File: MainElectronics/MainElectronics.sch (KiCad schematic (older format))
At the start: 15 parts

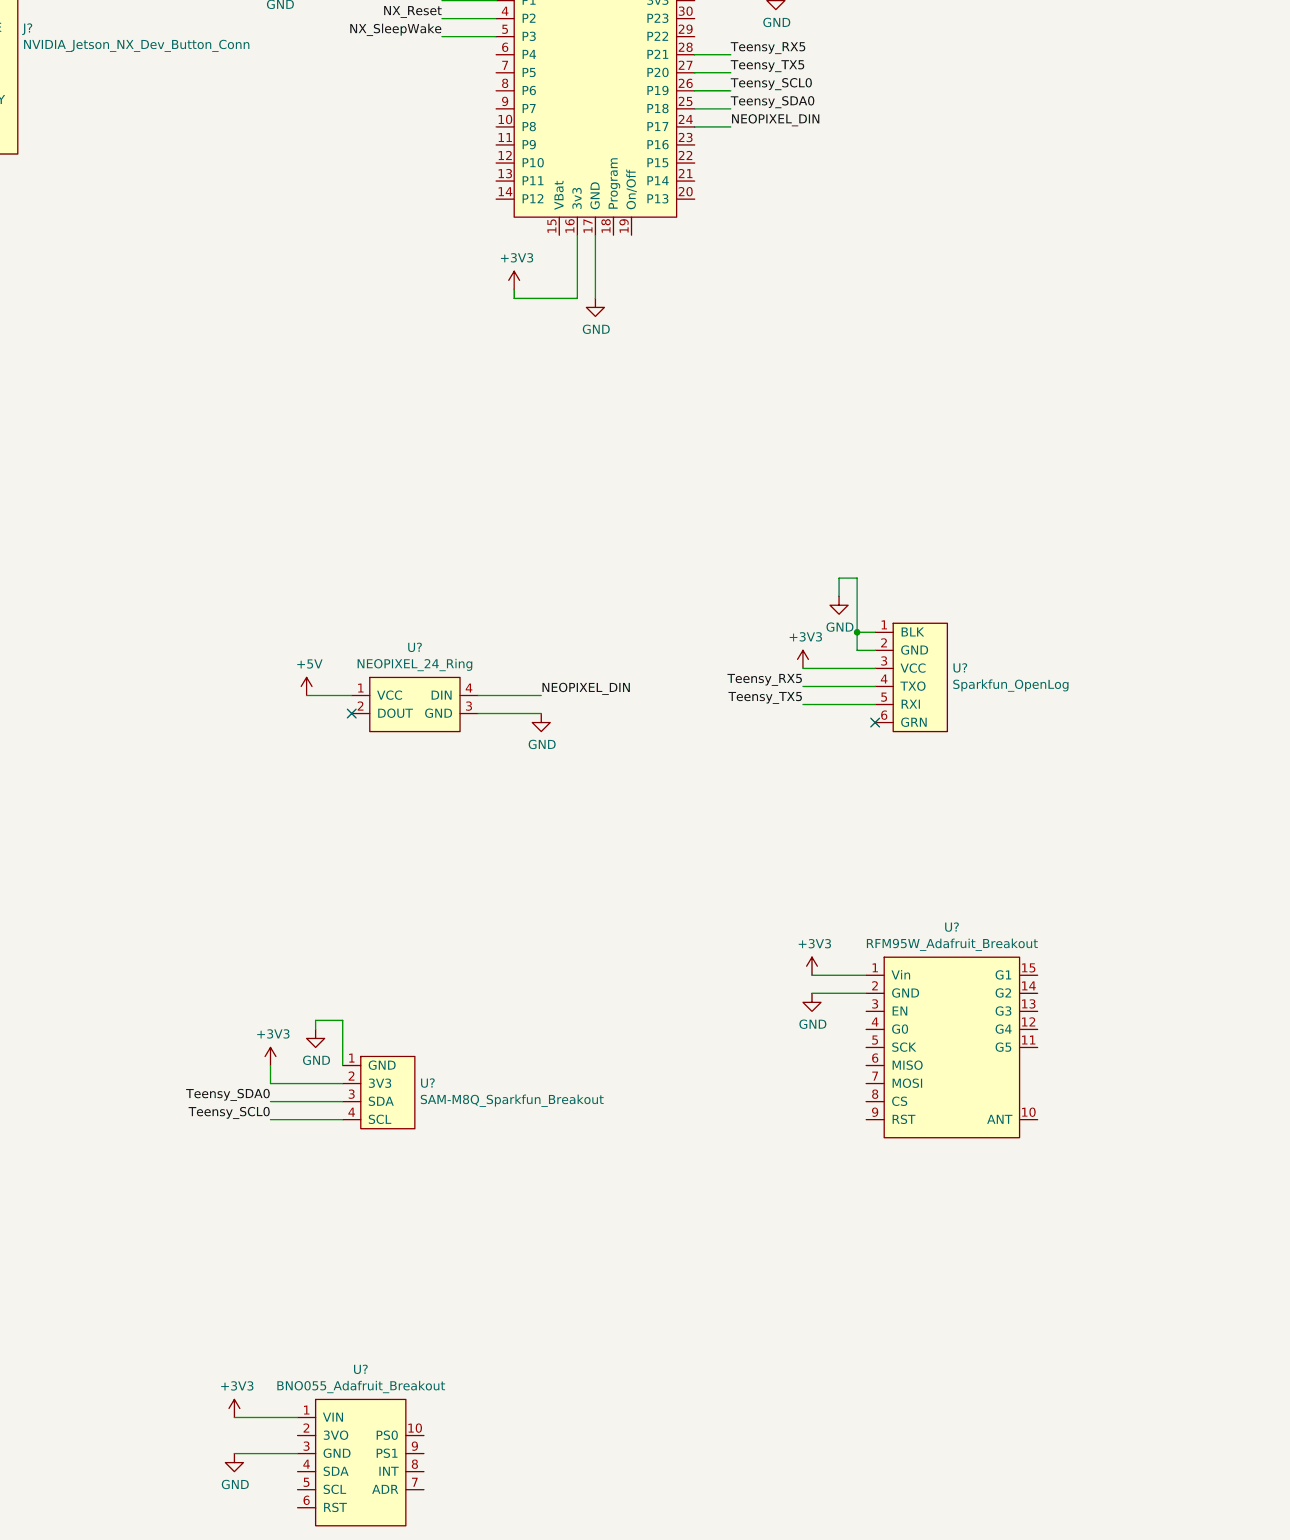
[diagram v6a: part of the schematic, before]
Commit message: Finished BNO055 and RFM95W
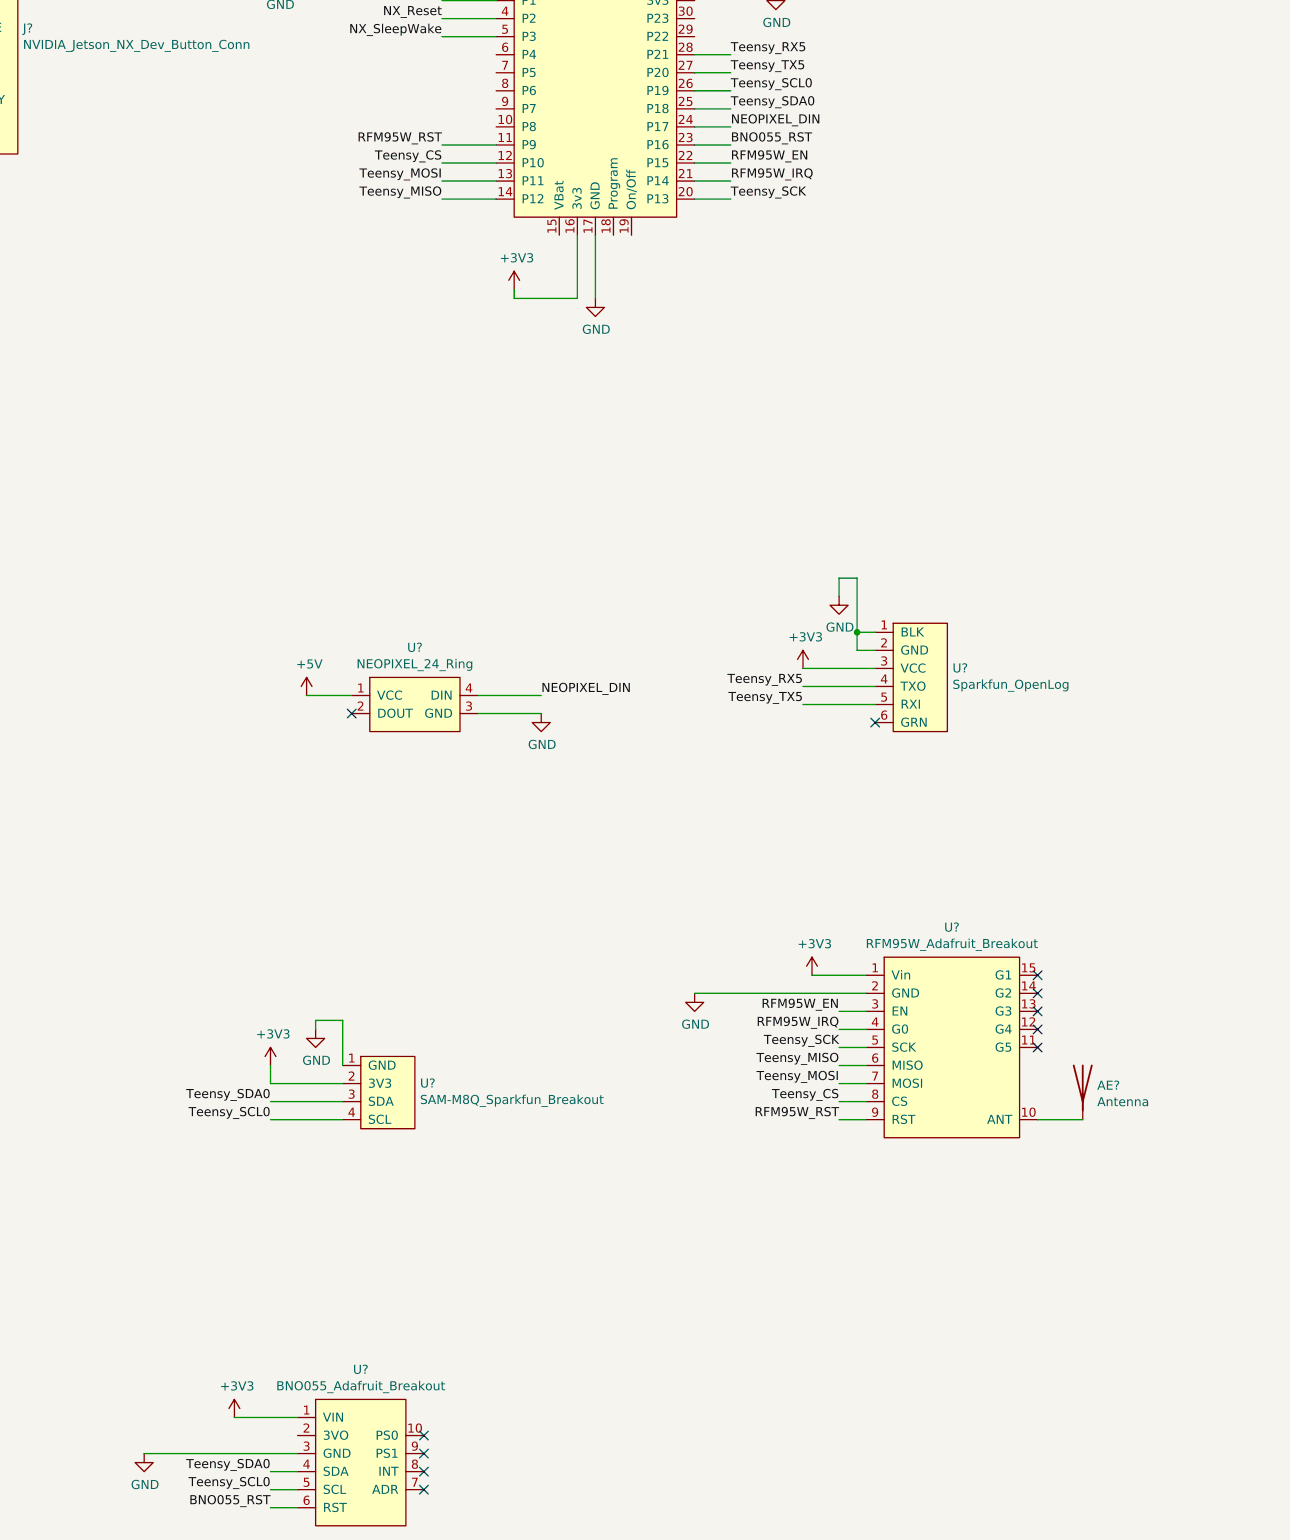
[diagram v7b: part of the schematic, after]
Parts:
- added AE?: Antenna, symbol Device:Antenna
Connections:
- net Teensy_SCL0: now also U?.5 (SCL)
- net Teensy_SDA0: now also U?.4 (SDA)
- net at U?.10 (ANT): now also AE?.1 (A)
- net RFM95W_EN: now reaches U?.3 (EN)
- net RFM95W_EN: now also U?.22 (P15)
- net RFM95W_IRQ: now reaches U?.4 (G0)
- net RFM95W_IRQ: now also U?.21 (P14)
- net Teensy_SCK: now reaches U?.5 (SCK)
- net Teensy_SCK: now also U?.20 (P13)
- net Teensy_MISO: now reaches U?.6 (MISO)
- net Teensy_MISO: now also U?.14 (P12)
- net Teensy_MOSI: now reaches U?.7 (MOSI)
- net Teensy_MOSI: now also U?.13 (P11)
- net Teensy_CS: now reaches U?.8 (CS)
- net Teensy_CS: now also U?.12 (P10)
- net RFM95W_RST: now reaches U?.9 (RST)
- net RFM95W_RST: now also U?.11 (P9)
- net BNO055_RST: now reaches U?.6 (RST)
- net BNO055_RST: now also U?.23 (P16)
- no-connect marks 4 -> 13
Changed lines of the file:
@@
 L power:GND #PWR?
 U 1 1 5EE0F934
-P 11500 7800
-F 0 "#PWR?" H 11500 7550 50  0001 C CNN
-F 1 "GND" H 11505 7627 50  0000 C CNN
-F 2 "" H 11500 7800 50  0001 C CNN
-F 3 "" H 11500 7800 50  0001 C CNN
-	1    11500 7800
-	1    0    0    -1
-$EndComp
-Wire Wire Line
-	11500 7800 11800 7800
+P 10850 7800
+F 0 "#PWR?" H 10850 7550 50  0001 C CNN
+F 1 "GND" H 10855 7627 50  0000 C CNN
+F 2 "" H 10850 7800 50  0001 C CNN
+F 3 "" H 10850 7800 50  0001 C CNN
+	1    10850 7800
+	1    0    0    -1
+$EndComp
+Wire Wire Line
+	10850 7800 11800 7800
 $Comp
 L power:+3V3 #PWR?
@@
 L power:GND #PWR?
 U 1 1 5EE15824
-P 8300 10350
-F 0 "#PWR?" H 8300 10100 50  0001 C CNN
-F 1 "GND" H 8305 10177 50  0000 C CNN
-F 2 "" H 8300 10350 50  0001 C CNN
-F 3 "" H 8300 10350 50  0001 C CNN
-	1    8300 10350
-	1    0    0    -1
-$EndComp
-Wire Wire Line
-	8650 10350 8300 10350
+P 7800 10350
+F 0 "#PWR?" H 7800 10100 50  0001 C CNN
+F 1 "GND" H 7805 10177 50  0000 C CNN
+F 2 "" H 7800 10350 50  0001 C CNN
+F 3 "" H 7800 10350 50  0001 C CNN
+	1    7800 10350
+	1    0    0    -1
+$EndComp
+Wire Wire Line
+	8650 10350 7800 10350
 Wire Wire Line
 	11850 6100 11450 6100
@@
 Text Label 8500 8400 2    50   ~ 0
 Teensy_SDA0
+Text Label 8500 10550 2    50   ~ 0
+Teensy_SCL0
+Wire Wire Line
+	8500 10550 8650 10550
+Text Label 8500 10450 2    50   ~ 0
+Teensy_SDA0
+Wire Wire Line
+	8500 10450 8650 10450
+Text Label 8500 10650 2    50   ~ 0
+BNO055_RST
+Wire Wire Line
+	8500 10650 8650 10650
+Text Label 11050 3100 0    50   ~ 0
+BNO055_RST
+Wire Wire Line
+	11050 3100 10850 3100
+Text Label 9450 3200 2    50   ~ 0
+Teensy_CS
+Text Label 9450 3300 2    50   ~ 0
+Teensy_MOSI
+Text Label 9450 3400 2    50   ~ 0
+Teensy_MISO
+Text Label 11050 3400 0    50   ~ 0
+Teensy_SCK
+Wire Wire Line
+	11050 3400 10850 3400
+Wire Wire Line
+	9750 3400 9450 3400
+Wire Wire Line
+	9450 3300 9750 3300
+Wire Wire Line
+	9750 3200 9450 3200
+Text Label 11650 8400 2    50   ~ 0
+Teensy_CS
+Wire Wire Line
+	11650 8400 11800 8400
+Text Label 11650 8300 2    50   ~ 0
+Teensy_MOSI
+Wire Wire Line
+	11650 8300 11800 8300
+Text Label 11650 8200 2    50   ~ 0
+Teensy_MISO
+Wire Wire Line
+	11650 8200 11800 8200
+Text Label 11650 8100 2    50   ~ 0
+Teensy_SCK
+Wire Wire Line
+	11650 8100 11800 8100
+Text Label 11650 7900 2    50   ~ 0
+RFM95W_EN
+Text Label 11650 8000 2    50   ~ 0
+RFM95W_IRQ
+Text Label 11650 8500 2    50   ~ 0
+RFM95W_RST
+Wire Wire Line
+	11650 8500 11800 8500
+Wire Wire Line
+	11800 8000 11650 8000
+Wire Wire Line
+	11650 7900 11800 7900
+$Comp
+L Device:Antenna AE?
+U 1 1 5F3457FE
+P 13000 8300
+F 0 "AE?" H 13080 8289 50  0000 L CNN
+F 1 "Antenna" H 13080 8198 50  0000 L CNN
+F 2 "" H 13000 8300 50  0001 C CNN
+F 3 "~" H 13000 8300 50  0001 C CNN
+	1    13000 8300
+	1    0    0    -1
+$EndComp
+Wire Wire Line
+	13000 8500 12750 8500
+NoConn ~ 12750 8100
+NoConn ~ 12750 8000
+NoConn ~ 12750 7900
+NoConn ~ 12750 7800
+NoConn ~ 12750 7700
+Text Label 11050 3200 0    50   ~ 0
+RFM95W_EN
+Text Label 11050 3300 0    50   ~ 0
+RFM95W_IRQ
+Wire Wire Line
+	11050 3300 10850 3300
+Wire Wire Line
+	10850 3200 11050 3200
+Text Label 9450 3100 2    50   ~ 0
+RFM95W_RST
+Wire Wire Line
+	9450 3100 9750 3100
+NoConn ~ 9350 10550
+NoConn ~ 9350 10450
+NoConn ~ 9350 10350
+NoConn ~ 9350 10250
 $EndSCHEMATC

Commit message: Added motor drivers
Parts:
- added M? (x8): Motor_DC, symbol Motor:Motor_DC
- added R?: 10k, symbol Device:R
- added U?: Teensy_4.0_Backside, symbol MainElectronicsLib:Teensy_4.0_Backside
- added U? (x8): MAX14870_Breakout, symbol MainElectronicsLib:MAX14870_Breakout
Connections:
- net GND is gone; now on net -BATT: J?.11 (GND), J?.14 (GND), J?.20 (GND), J?.25 (GND), J?.30 (GND), J?.34 (GND), J?.39 (GND), J?.6 (GND), J?.7 (GND), J?.9 (GND), J?.9 (GND), Q?.3 (S), Q?.3 (S), R?.1, R?.1, U?.1 (BLK), U?.1 (GND), U?.1 (GND), U?.17 (GND), U?.2 (GND), U?.2 (GND), U?.3 (GND), U?.3 (GND), U?.32 (GND)
- net +3V3: now also R?.1
- net +BATT: now also U?.7 (VIN), U?.7 (VIN), U?.7 (VIN), U?.7 (VIN), U?.7 (VIN), U?.7 (VIN), U?.7 (VIN), U?.7 (VIN)
- net -BATT: now also U?.5 (GND), U?.5 (GND), U?.5 (GND), U?.5 (GND), U?.5 (GND), U?.5 (GND), U?.5 (GND), U?.5 (GND), U?.6 (GND), U?.6 (GND), U?.6 (GND), U?.6 (GND), U?.6 (GND), U?.6 (GND), U?.6 (GND), U?.6 (GND)
- net NX_Reset: no longer Q?.2 (G), R?.2
- net Fault_Common: now reaches U?.10 (P8)
- net Fault_Common: now also R?.2, U?.3 (~FAULT), U?.3 (~FAULT), U?.3 (~FAULT), U?.3 (~FAULT), U?.3 (~FAULT), U?.3 (~FAULT), U?.3 (~FAULT), U?.3 (~FAULT)
- net MOTOR_3_DIR: now reaches U?.29 (P22)
- net MOTOR_3_DIR: now also U?.2 (DIR)
- net MOTOR_3_PWM: now reaches U?.30 (P23)
- net MOTOR_3_PWM: now also U?.1 (PWM)
- net MOTOR_1_PWM: now reaches U?.6 (P4)
- net MOTOR_1_PWM: now also U?.1 (PWM)
- net MOTOR_1_DIR: now reaches U?.7 (P5)
- net MOTOR_1_DIR: now also U?.2 (DIR)
- net MOTOR_2_PWM: now reaches U?.8 (P6)
- net MOTOR_2_PWM: now also U?.1 (PWM)
- net MOTOR_2_DIR: now reaches U?.9 (P7)
- net MOTOR_2_DIR: now also U?.2 (DIR)
- new net: Q?.2 (G), R?.2
- new net: M?.2 (-), U?.8 (M2) (x8)
- new net: M?.1 (+), U?.9 (M1) (x8)
- new net MOTOR_4_DIR: U?.2 (DIR), U?.2 (P26)
- new net MOTOR_4_PWM: U?.1 (P24), U?.1 (PWM)
- new net MOTOR_5_DIR: U?.2 (DIR), U?.4 (P30)
- new net MOTOR_5_PWM: U?.1 (PWM), U?.3 (P28)
- new net MOTOR_6_DIR: U?.2 (DIR), U?.9 (P27)
- new net MOTOR_6_PWM: U?.1 (PWM), U?.10 (P25)
- new net MOTOR_7_DIR: U?.2 (DIR), U?.7 (P31)
- new net MOTOR_7_PWM: U?.1 (PWM), U?.8 (P29)
- new net MOTOR_8_DIR: U?.2 (DIR), U?.5 (P32)
- new net MOTOR_8_PWM: U?.1 (PWM), U?.6 (P33)
- no-connect marks 13 -> 29
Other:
- moved on the sheet: AE?, BT?, J?, Q?, R?, SW?, U?
